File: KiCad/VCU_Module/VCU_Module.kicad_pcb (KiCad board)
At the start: 4 copper layers, 85.1 x 64.6 mm, 44 parts, among them IC1 STM32C092RCT6, J1 5810132011, J11 Conn_ST_STDC14, J5 pin header, J7 5V, J8 3V3, J9 GND, Q1 AO3401A, SW2 SW_Push, U1 OKI-78SR-5_1.5-W36-C, U2 TLV75533PDBV, U6 MCP2562FDT-H_SN

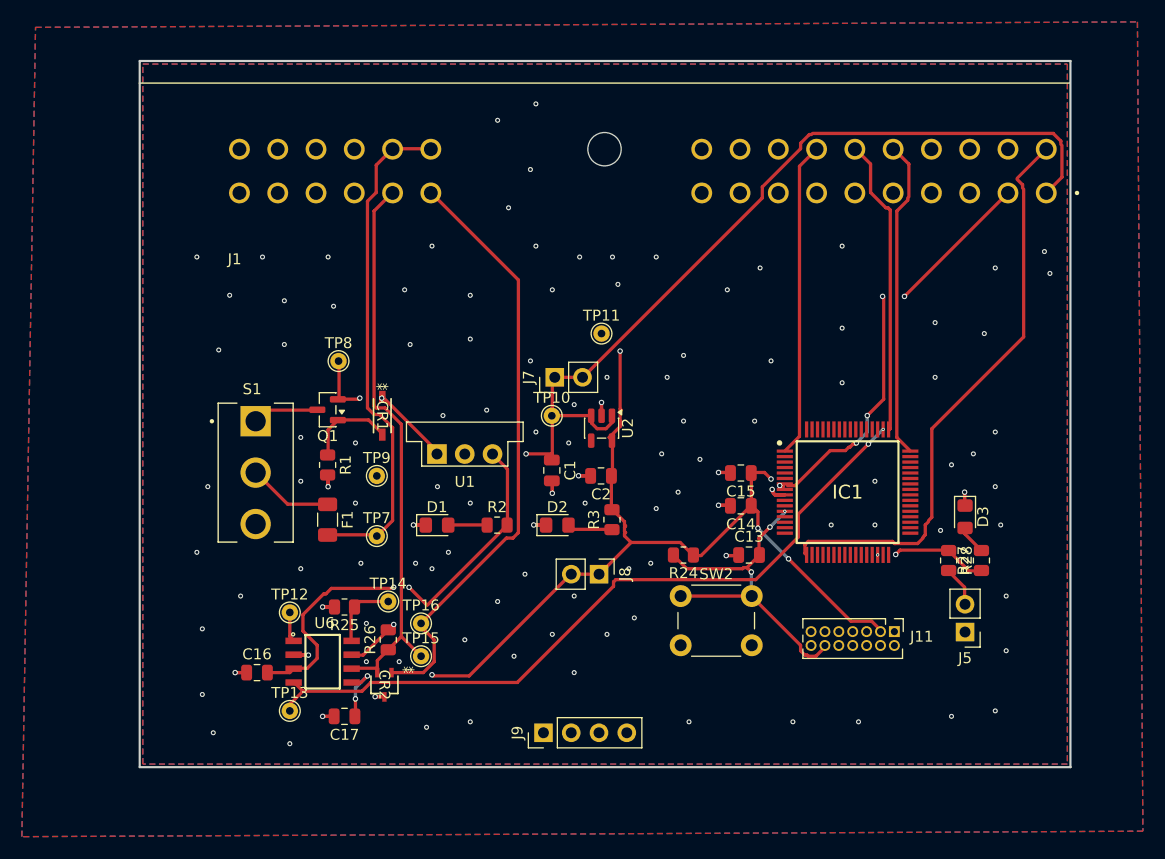
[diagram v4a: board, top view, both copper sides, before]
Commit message: fixed all socket header connections, placed and routed every component on PCB, added all 3d models to footprints
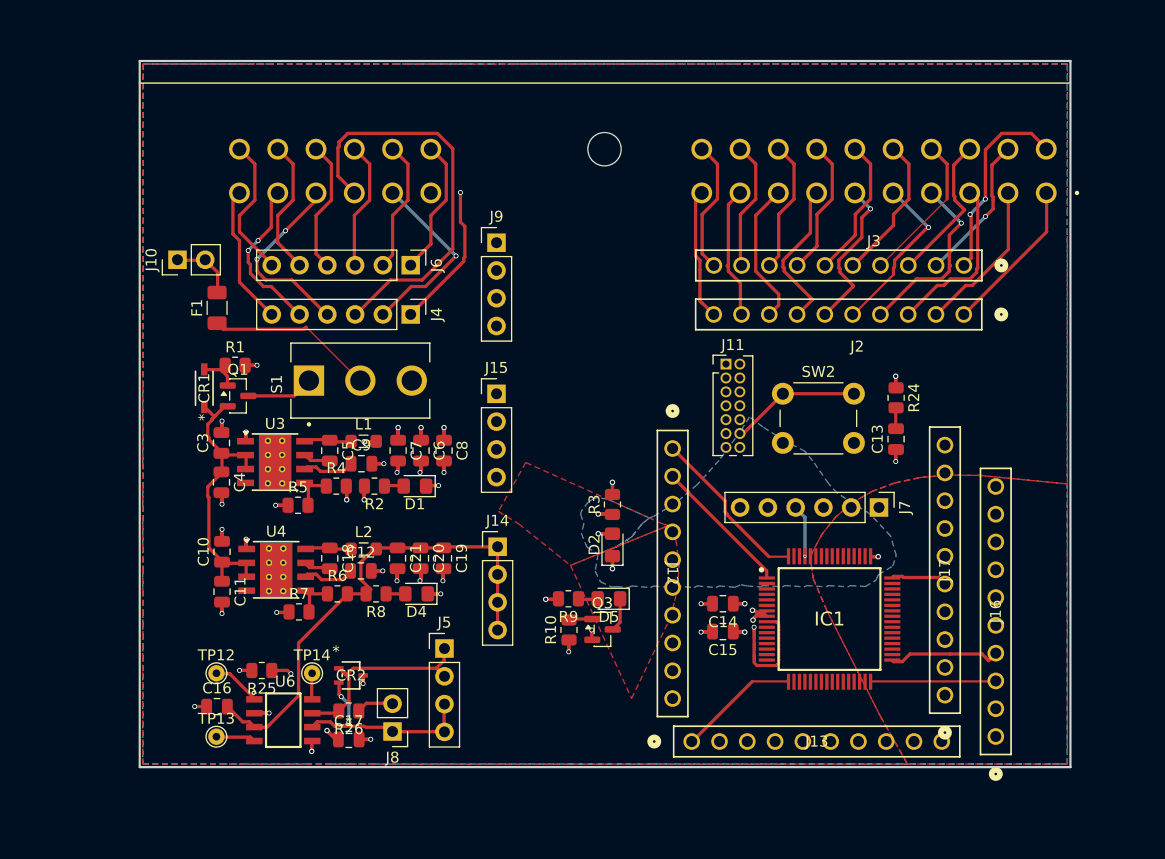
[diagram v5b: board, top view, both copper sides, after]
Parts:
- removed C1, C2: 10u, Capacitor_SMD:C_0805_2012Metric
- removed D3: LED, LED_SMD:LED_0805_2012Metric_Pad1.15x1.40mm_HandSolder
- removed R27, R28: 1k, Resistor_SMD:R_0805_2012Metric
- removed TP10, TP11, TP15, TP16, TP7, TP8, TP9: TestPoint_Small, TestPoint:TestPoint_THTPad_D1.5mm_Drill0.7mm
- removed U1: OKI-78SR-5_1.5-W36-C, Converter_DCDC:Converter_DCDC_Murata_OKI-78SR_Vertical
- removed U2: TLV75533PDBV, Package_TO_SOT_SMD:SOT-23-5
- added C10: 10u, Capacitor_SMD:C_0805_2012Metric, F.Cu at (182.8, 88.5)
- added C11: 220n, Capacitor_SMD:C_0805_2012Metric, F.Cu at (182.8, 92.1)
- added C12: 1u, Capacitor_SMD:C_0805_2012Metric, F.Cu at (195.5, 90.2)
- added C18: 0.1u, Capacitor_SMD:C_0805_2012Metric, F.Cu at (192.7, 89.0)
- added C19: 22u, Capacitor_SMD:C_0805_2012Metric, F.Cu at (203.1, 89.0)
- added C20: 22u, Capacitor_SMD:C_0805_2012Metric, F.Cu at (200.9, 89.0)
- added C21: 22u, Capacitor_SMD:C_0805_2012Metric, F.Cu at (198.8, 89.0)
- added C3: 10u, Capacitor_SMD:C_0805_2012Metric, F.Cu at (182.8, 78.5)
- added C4: 220n, Capacitor_SMD:C_0805_2012Metric, F.Cu at (182.8, 82.1)
- added C5: 0.1u, Capacitor_SMD:C_0805_2012Metric, F.Cu at (192.7, 79.2)
- added C6: 22u, Capacitor_SMD:C_0805_2012Metric, F.Cu at (201.0, 79.2)
- added C7: 22u, Capacitor_SMD:C_0805_2012Metric, F.Cu at (198.9, 79.2)
- added C8: 22u, Capacitor_SMD:C_0805_2012Metric, F.Cu at (203.1, 79.2)
- added C9: 1u, Capacitor_SMD:C_0805_2012Metric, F.Cu at (195.6, 80.4)
- added D4: GRN, LED_SMD:LED_0805_2012Metric_Pad1.15x1.40mm_HandSolder, F.Cu at (200.6, 92.3)
- added D5: GRN, LED_SMD:LED_0805_2012Metric_Pad1.15x1.40mm_HandSolder, F.Cu at (218.2, 92.8)
- added J10: 12V, Connector_PinHeader_2.54mm:PinHeader_1x02_P2.54mm_Vertical, F.Cu at (178.7, 61.8)
- added J12: MCU1, VMS_Footprints:1x10_Header_f, F.Cu at (224.0, 79.0)
- added J13: MCU2, VMS_Footprints:1x10_Header_f, F.Cu at (225.8, 105.8)
- added J14: 5V, Connector_PinHeader_2.54mm:PinHeader_1x04_P2.54mm_Vertical, F.Cu at (208.0, 88.0)
- added J15: 3V3, Connector_PinHeader_2.54mm:PinHeader_1x04_P2.54mm_Vertical, F.Cu at (207.9, 74.0)
- added J16: MCU3, VMS_Footprints:1x10_Header_f, F.Cu at (253.6, 105.3)
- added J17: MCU4, VMS_Footprints:1x10_Header_f, F.Cu at (248.9, 101.6)
- added J2: CN1, VMS_Footprints:1x10_Header_f, F.Cu at (250.6, 66.8)
- added J3: CN2, VMS_Footprints:1x10_Header_f, F.Cu at (250.6, 62.3)
- added J4: CN3, Connector_PinHeader_2.54mm:PinHeader_1x06_P2.54mm_Vertical, F.Cu at (200.1, 66.8)
- added J6: CN4, Connector_PinHeader_2.54mm:PinHeader_1x06_P2.54mm_Vertical, F.Cu at (200.1, 62.2)
- added L1: 3.3u, Inductor_SMD:L_0805_2012Metric_Pad1.05x1.20mm_HandSolder, F.Cu at (195.8, 78.3)
- added L2: 3.3u, Inductor_SMD:L_0805_2012Metric_Pad1.05x1.20mm_HandSolder, F.Cu at (195.8, 88.2)
- added Q3: 2N7002, Package_TO_SOT_SMD:SOT-23, F.Cu at (217.6, 95.5)
- added R10: 1M, Resistor_SMD:R_0805_2012Metric, F.Cu at (214.5, 95.6)
- added R4: 100k, Resistor_SMD:R_0805_2012Metric, F.Cu at (193.2, 82.5)
- added R5: 43.2k, Resistor_SMD:R_0805_2012Metric, F.Cu at (189.8, 84.2)
- added R6: 100k, Resistor_SMD:R_0805_2012Metric, F.Cu at (193.3, 92.3)
- added R7: 43.2k, Resistor_SMD:R_0805_2012Metric, F.Cu at (189.8, 94.0)
- added R8: 1k, Resistor_SMD:R_0805_2012Metric, F.Cu at (196.9, 92.3)
- added R9: 680, Resistor_SMD:R_0805_2012Metric, F.Cu at (214.5, 92.8)
- added U3: LMR33640DDDA, Package_SO:Texas_HSOP-8-1EP_3.9x4.9mm_P1.27mm_ThermalVias, F.Cu at (187.7, 80.2)
- added U4: LMR33640DDDA, Package_SO:Texas_HSOP-8-1EP_3.9x4.9mm_P1.27mm_ThermalVias, F.Cu at (187.8, 90.1)
- D2: value GRN -> Blue
- J5: value pin header -> MCU6; footprint Connector_PinHeader_2.54mm:PinHeader_1x02_P2.54mm_Vertical -> Connector_PinHeader_2.54mm:PinHeader_1x04_P2.54mm_Vertical
- J7: value 5V -> MCU5; footprint Connector_PinHeader_2.54mm:PinHeader_1x02_P2.54mm_Vertical -> Connector_PinHeader_2.54mm:PinHeader_1x06_P2.54mm_Vertical
- J8: value 3V3 -> Termination Resistor Jumper
- R3: value 1k -> 360
- moved J5 47.6 mm to (203.1, 97.3), turned to 0 degrees
- moved J9 45.0 mm to (207.9, 60.2), turned to 0 degrees
- moved J7 31.9 mm to (242.9, 84.4), turned to -90 degrees
- moved J11 28.9 mm to (228.9, 71.3), turned to 0 degrees
- moved R24 24.2 mm to (244.4, 74.4), turned to -90 degrees
- moved J8 23.7 mm to (198.4, 104.9), turned to 180 degrees
- moved F1 21.8 mm to (182.3, 66.2), turned to 90 degrees
- moved SW2 20.7 mm to (234.1, 74.0)
- moved C13 17.1 mm to (244.4, 78.2), turned to 90 degrees
- moved CR1 16.5 mm to (181.2, 73.5), turned to 90 degrees
- moved C15 14.6 mm to (228.6, 95.8)
- moved S1 12.7 mm to (195.4, 72.8), turned to 90 degrees
- moved R1 12.4 mm to (184.0, 71.4), turned to 0 degrees
- moved R2 11.8 mm to (196.7, 82.5), turned to 180 degrees
- moved IC1 11.7 mm to (238.3, 94.6)
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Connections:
- net /POWER/VIN_PROTECTED renamed /VIN_PROTECTED
- C13 pad 2: Net-(IC1-PF2-NRST) -> Net-(C13-Pad2)
- D2 pad 1: GND -> /MCU/PC9/User LED 2
- F1 pad 2: +12V -> VDD
- IC1 pad 1: /A17 -> /MCU/PC11/TIM1_CH4
- IC1 pad 13: unconnected-(IC1-PC0-Pad13) -> /MCU/PC0
- IC1 pad 14: unconnected-(IC1-PC1-Pad14) -> /MCU/PC1
- IC1 pad 15: unconnected-(IC1-PC2-Pad15) -> /MCU/PC2
- IC1 pad 16: unconnected-(IC1-PC3-Pad16) -> /MCU/PC3
- IC1 pad 17: /A11 -> /MCU/PA0/ADC0
- IC1 pad 18: /A12 -> /MCU/PA1/ADC1
- IC1 pad 2: unconnected-(IC1-PC12-Pad2) -> /MCU/PC12
- IC1 pad 21: /A13 -> /MCU/PA4/ADC4
- IC1 pad 22: /A8 -> /MCU/PA5/User LED 1
- IC1 pad 23: /A5 -> /MCU/PA6/SPI1_MISO
- IC1 pad 24: /A6 -> /MCU/PA7/SPI1_MOSI
- IC1 pad 25: /A19 -> /MCU/PC4/TIM2_CH1
- IC1 pad 26: /A20 -> /MCU/PC5/TIM2_CH2
- IC1 pad 27: unconnected-(IC1-PB0-Pad27) -> /MCU/PB0
- IC1 pad 28: unconnected-(IC1-PB1-Pad28) -> /MCU/PB1
- IC1 pad 29: unconnected-(IC1-PB2-Pad29) -> /MCU/PB2
- IC1 pad 3: /A18 -> /MCU/PC13/TIM1_ETR/BKIN
- IC1 pad 30: Net-(IC1-PB10) -> unconnected-(IC1-PB10-Pad30)
- IC1 pad 31: unconnected-(IC1-PB11-Pad31) -> /MCU/PB11
- IC1 pad 32: unconnected-(IC1-PB12-Pad32) -> /MCU/PB12
- IC1 pad 33: unconnected-(IC1-PB13-Pad33) -> /MCU/PB13
- IC1 pad 34: unconnected-(IC1-PB14-Pad34) -> /MCU/PB14
- IC1 pad 35: unconnected-(IC1-PB15-Pad35) -> /MCU/PB15
- IC1 pad 36: /A14 -> /MCU/PA8/ADC8
- IC1 pad 37: /A3 -> /MCU/PA9/I2C1_SCL
- IC1 pad 38: unconnected-(IC1-PC6-Pad38) -> /MCU/PC6
- IC1 pad 39: unconnected-(IC1-PC7-Pad39) -> /MCU/PC7
- IC1 pad 4: unconnected-(IC1-PC14-OSCX_IN-Pad4) -> /MCU/PC14
- IC1 pad 40: unconnected-(IC1-PD8-Pad40) -> /MCU/PD8
- IC1 pad 41: unconnected-(IC1-PD9-Pad41) -> /MCU/PD9
- IC1 pad 42: /A4 -> /MCU/PA10/I2C1_SDA
- IC1 pad 47: /A7 -> /MCU/PA15/SPI1_NSS
- IC1 pad 48: /A15 -> /MCU/PC8/TIM1_CH1
- IC1 pad 49: /A16 -> /MCU/PC9/User LED 2
- IC1 pad 5: unconnected-(IC1-PC15-OSCX_OUT-Pad5) -> /MCU/PC15
- IC1 pad 53: unconnected-(IC1-PD3-Pad53) -> /MCU/PD3
- IC1 pad 54: unconnected-(IC1-PD4-Pad54) -> /MCU/PD4
- IC1 pad 55: unconnected-(IC1-PD5-Pad55) -> /MCU/PD5
- IC1 pad 56: unconnected-(IC1-PD6-Pad56) -> /MCU/PD6
- IC1 pad 58: unconnected-(IC1-PB4-Pad58) -> /MCU/PB4
- IC1 pad 59: unconnected-(IC1-PB5-Pad59) -> /MCU/PB5
- IC1 pad 60: /MCU/GPIO_SPARE1_PB6 -> /MCU/PB6/GPIO_SPARE1
- IC1 pad 61: /MCU/GPIO_SPARE2_PB7 -> /MCU/PB7/GPIO_SPARE2
- IC1 pad 62: /MCU/GPIO_SPARE3_PB8 -> /MCU/PB8/GPIO_SPARE3
- IC1 pad 63: /MCU/GPIO_SPARE4_PB9 -> /MCU/PB9/GPIO_SPARE4
- IC1 pad 64: unconnected-(IC1-PC10-Pad64) -> /MCU/PC10
- J1 pad A1: +5V -> Net-(J2-Pin_1)
- J1 pad A10: GND -> Net-(J2-Pin_10)
- J1 pad A11: /A11 -> Net-(J3-Pin_1)
- J1 pad A12: /A12 -> Net-(J3-Pin_2)
- J1 pad A13: /A13 -> Net-(J3-Pin_3)
- J1 pad A14: /A14 -> Net-(J3-Pin_4)
- J1 pad A15: /A15 -> Net-(J3-Pin_5)
- J1 pad A16: /A16 -> Net-(J3-Pin_6)
- J1 pad A17: /A17 -> Net-(J3-Pin_7)
- J1 pad A18: /A18 -> Net-(J3-Pin_8)
- J1 pad A19: /A19 -> Net-(J3-Pin_9)
- J1 pad A2: +3V3 -> Net-(J2-Pin_2)
- J1 pad A20: /A20 -> Net-(J3-Pin_10)
- J1 pad A3: /A3 -> Net-(J2-Pin_3)
- J1 pad A4: /A4 -> Net-(J2-Pin_4)
- J1 pad A5: /A5 -> Net-(J2-Pin_5)
- J1 pad A6: /A6 -> Net-(J2-Pin_6)
- J1 pad A7: /A7 -> Net-(J2-Pin_7)
- J1 pad A8: /A8 -> Net-(J2-Pin_8)
- J1 pad A9: GND -> Net-(J2-Pin_9)
- J1 pad B1: /MCU/CANH -> Net-(J4-Pin_1)
- J1 pad B10: unconnected-(J1-PadB10) -> Net-(J6-Pin_4)
- J1 pad B11: GND -> Net-(J6-Pin_5)
- J1 pad B12: GND -> Net-(J6-Pin_6)
- J1 pad B2: /MCU/CANL -> Net-(J4-Pin_2)
- J1 pad B3: /MCU/GPIO_SPARE1_PB6 -> Net-(J4-Pin_3)
- J1 pad B4: /MCU/GPIO_SPARE2_PB7 -> Net-(J4-Pin_4)
- J1 pad B5: /MCU/GPIO_SPARE4_PB9 -> Net-(J4-Pin_5)
- J1 pad B6: /MCU/GPIO_SPARE3_PB8 -> Net-(J4-Pin_6)
- J1 pad B7: +12V -> Net-(J6-Pin_1)
- J1 pad B8: +12V -> Net-(J6-Pin_2)
- J1 pad B9: unconnected-(J1-PadB9) -> Net-(J6-Pin_3)
- J5 pad 1: GND -> /MCU/CANH
- J5 pad 2: /MCU/FAULT_LED -> /MCU/CANH
- J7 pad 1: +5V -> /MCU/PB4
- J7 pad 2: +5V -> /MCU/PB5
- J8 pad 1: +3V3 -> /MCU/CANL
- J8 pad 2: +3V3 -> Net-(J8-Pin_2)
- R2 pad 2: +5V -> +3V3
- R24 pad 2: Net-(IC1-PF2-NRST) -> Net-(C13-Pad2)
- R26 pad 1: /MCU/CANL -> Net-(J8-Pin_2)
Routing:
- net +3V3: track 133.0 -> 18.1 mm, vias 12 -> 15
- net +5V: track 122.3 -> 45.7 mm, vias 3 -> 0
- net /MCU/CAN_RXD: track 67.8 -> 3.71 mm, vias 2 -> 0
- net /A11: track 52.6 -> 0.00 mm
- net +12V: track 46.1 -> 0.00 mm
- net /MCU/CANH: track 62.3 -> 19.0 mm, vias 1 -> 0
- net Net-(J4-Pin_3): track 0.00 -> 37.2 mm
- net /MCU/CANL: track 52.1 -> 19.7 mm, vias 0 -> 2
- net /A15: track 29.1 -> 0.00 mm
- net /A17: track 28.9 -> 0.00 mm
- net /A16: track 27.2 -> 0.00 mm
- net Net-(IC1-PF2-NRST): track 32.8 -> 12.0 mm, vias 3 -> 0
- net Net-(J3-Pin_1): track 0.00 -> 18.3 mm, vias 0 -> 2
- net Net-(J4-Pin_4): track 0.00 -> 17.5 mm, vias 0 -> 2
- net Net-(J4-Pin_2): track 0.00 -> 17.1 mm, vias 0 -> 1
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- added copper zone on B.Cu, net +3V3
- added copper zone on F.Cu, net +3V3
- added copper zone on B.Cu, net /MCU/PC9/User LED 2
- added copper zone on F.Cu, net /MCU/PC9/User LED 2
- added copper zone on B.Cu, net Net-(D2-A)
- added copper zone on F.Cu, net Net-(D2-A)
- removed copper zone on B.Cu, net (none)
- removed copper zone on F.Cu, net (none)
- removed copper zone on F.Cu, net GND

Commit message: updated pcb from sohams adjustments to schematic
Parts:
- removed S1: 100SP1T1B4M2QE, VMS_Footprints:SW_100SP1T1B4M2QE
- CR1: value MMSZ5245B-7-F -> MMSZ5240B
- Q1: value AO3401A -> SUD19P06-60; footprint Package_TO_SOT_SMD:SOT-23 -> Package_TO_SOT_SMD:TO-252-2
- R7: value 43.2k -> 24.9k
- moved Q1 8.78 mm to (192.9, 72.7)
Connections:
- CR1 pad 1: /VIN_PROTECTED -> Net-(Q1-S)
- F1 pad 1: Net-(F1-Pad1) -> Net-(Q1-S)
- Q1 pad 3: Net-(Q1-D) -> Net-(Q1-S)
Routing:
- net GND: track 35.4 -> 156.2 mm, vias 30 -> 8
- net /MCU/PC9/User LED 2: track 1.85 -> 29.2 mm
- net +3V3: track 18.1 -> 0.00 mm, vias 15 -> 0
- net Net-(F1-Pad1): track 15.4 -> 0.00 mm
- net /MCU/PC6: track 0.00 -> 15.1 mm, vias 0 -> 2
- net Net-(Q1-S): track 0.00 -> 14.8 mm, vias 0 -> 2
- net Net-(Q1-G): track 3.81 -> 18.2 mm
- net /MCU/PD5: track 0.00 -> 13.0 mm, vias 0 -> 2
- net /MCU/PA8/ADC8: track 0.00 -> 12.8 mm, vias 0 -> 2
- net /MCU/PD9: track 0.00 -> 11.3 mm, vias 0 -> 2
- net /MCU/PC13/TIM1_ETR/BKIN: track 0.00 -> 10.8 mm, vias 0 -> 2
- net /MCU/PB14: track 0.00 -> 10.6 mm, vias 0 -> 2
- net /VIN_PROTECTED: track 27.2 -> 37.5 mm
- net /MCU/PC3: track 0.00 -> 10.1 mm
- net /MCU/PC0: track 0.00 -> 9.39 mm, vias 0 -> 2
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
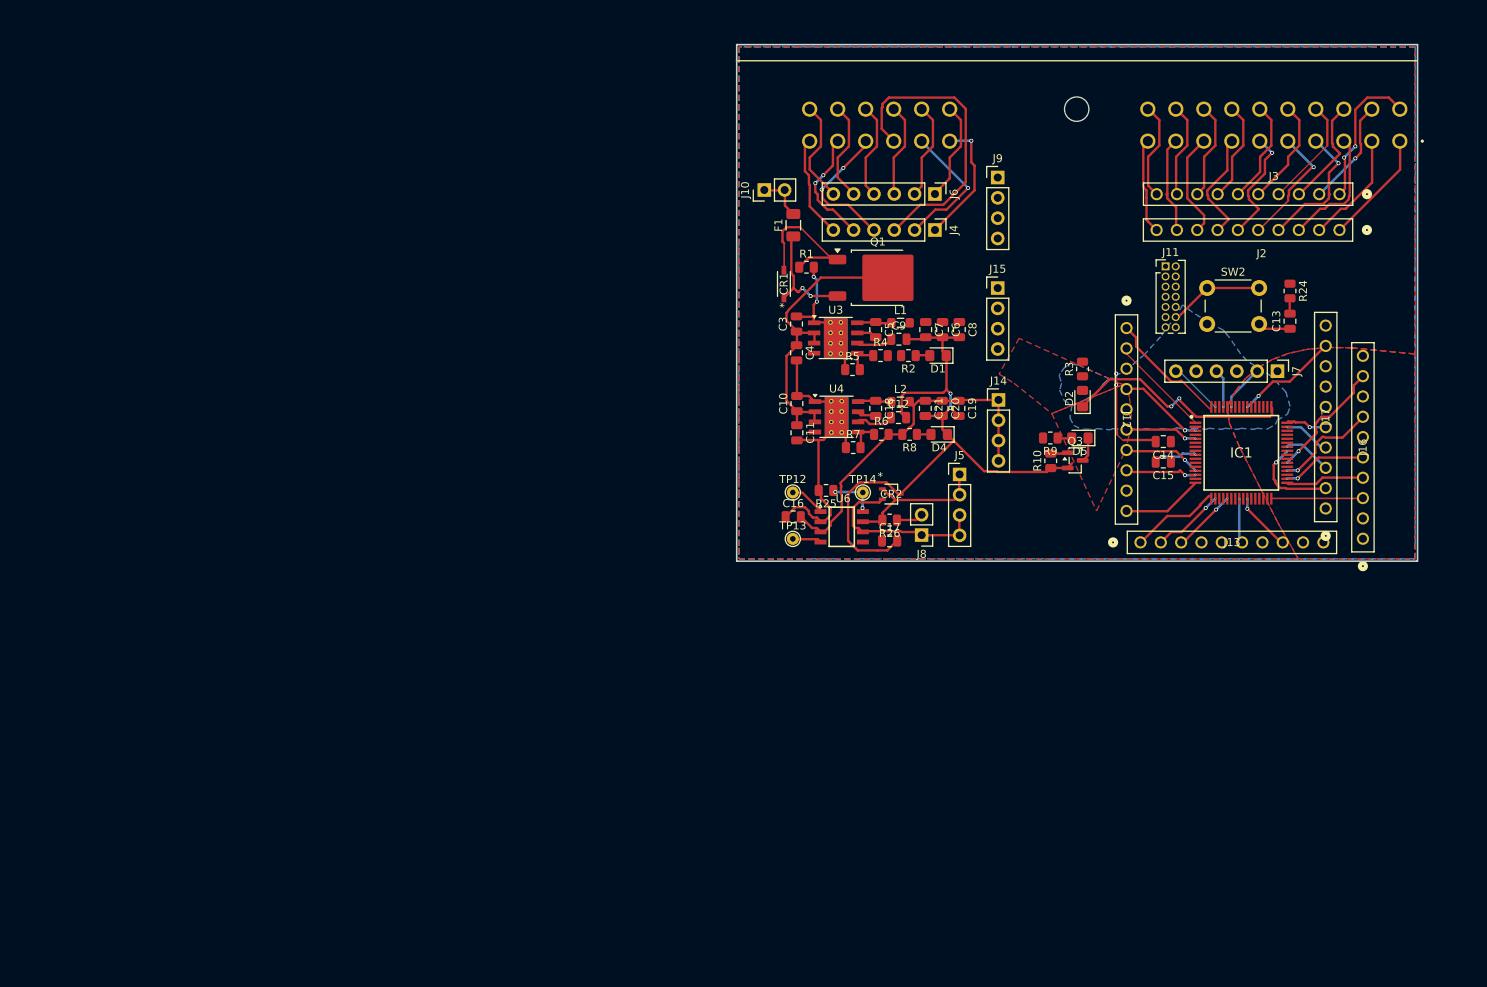
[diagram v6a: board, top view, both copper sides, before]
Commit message: schematic complete with new fuse holder and specs, just need to run ERC once more PCB component placement and traces done, still need to fix some DRC Errors and check warnings Still need to ensure all components are labeled properly with no overlapping silkscreen labels
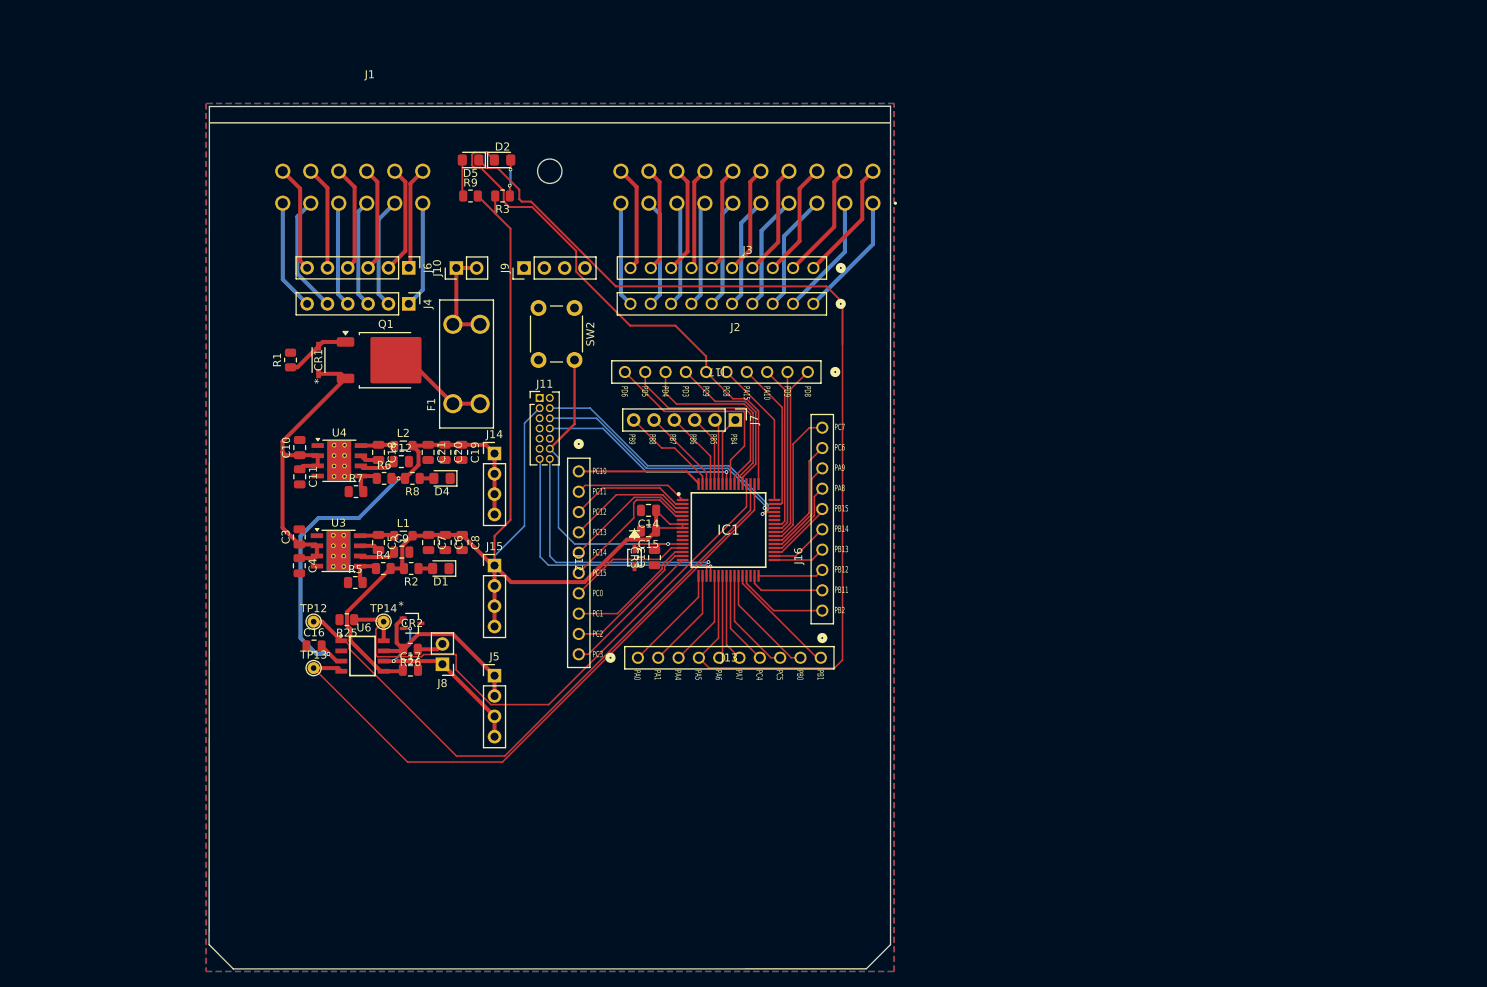
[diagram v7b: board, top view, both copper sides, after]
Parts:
- removed Q3: 2N7002, Package_TO_SOT_SMD:SOT-23
- removed R10: 1M, Resistor_SMD:R_0805_2012Metric
- removed R24: 10k, Resistor_SMD:R_0805_2012Metric
- added CR3: ESDA051-1JY, VMS_Footprints:ESDA051-1JY, F.Cu at (162.5, 107.7)
- F1: value Fuse -> 3568; footprint Fuse:Fuse_1206_3216Metric -> VMS_Footprints:FUSE_3568
- J1: footprint VMS_Footprints:CINCH_5810132011_30-pin -> VMS_Footprints:Cinch_5810132011_PCB_Header
- moved C13 84.7 mm to (165.0, 107.7)
- moved D5 83.7 mm to (142.0, 58.0)
- moved J11 80.0 mm to (150.6, 87.7)
- moved SW2 79.1 mm to (155.0, 76.5), turned to -90 degrees
- moved R9 78.5 mm to (142.0, 62.5), turned to 0 degrees
- moved D2 78.4 mm to (146.0, 58.0), turned to 0 degrees
- moved R3 75.7 mm to (146.0, 62.5), turned to 180 degrees
- moved J15 71.8 mm to (145.0, 108.7)
- moved J12 70.8 mm to (155.5, 96.9)
- moved J16 68.2 mm to (186.0, 114.3)
- moved J7 68.0 mm to (175.1, 90.5)
- moved C3 67.6 mm to (120.6, 105.1)
- moved C4 67.6 mm to (120.6, 108.7)
- moved C5 67.6 mm to (130.5, 105.8)
- moved C6 67.6 mm to (138.8, 105.8)
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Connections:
- net +3V3 renamed 3V3
- net +5V renamed 5V
- net /MCU/PB3 renamed /MCU/SWO
- net Net-(IC1-PA13) renamed /MCU/SWDIO
- net Net-(IC1-PA14-BOOT0) renamed /MCU/SWCLK/BOOT0
- C13 pad 2: Net-(C13-Pad2) -> /MCU/NRST
- CR1 pad 1: Net-(Q1-S) -> /VIN_PROTECTED
- D5 pad 1: Net-(D5-K) -> /MCU/PA5/User LED 1
- F1 pad 1: Net-(Q1-S) -> Net-(Q1-D)
- IC1 pad 12: Net-(IC1-PF2-NRST) -> /MCU/NRST
- IC1 pad 19: Net-(IC1-PA2) -> /MCU/VCP_TX
- IC1 pad 20: Net-(IC1-PA3) -> /MCU/VCP_RX
- J11 pad 12: Net-(IC1-PF2-NRST) -> /MCU/NRST
- J11 pad 13: Net-(IC1-PA2) -> /MCU/VCP_RX
- J11 pad 14: Net-(IC1-PA3) -> /MCU/VCP_TX
- J13 pad 4: /PA5/SPI1_SCK -> /MCU/PA5/User LED 1
- J17 pad 6: /PC9/TIM1_CH2 -> /MCU/PC9/User LED 2
- Q1 pad 2: /VIN_PROTECTED -> Net-(Q1-D)
- Q1 pad 3: Net-(Q1-S) -> /VIN_PROTECTED
- SW2 pad 1: Net-(IC1-PF2-NRST) -> /MCU/NRST
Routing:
- net GND: track 156.2 -> 0.00 mm, vias 8 -> 0
- net 3V3: track 0.00 -> 152.7 mm
- net /MCU/PA5/User LED 1: track 2.22 -> 128.4 mm
- net /MCU/CAN_RXD: track 3.77 -> 79.9 mm
- net /MCU/CAN_TXD: track 4.56 -> 77.8 mm
- net /MCU/STDBY: track 6.20 -> 74.1 mm, vias 2 -> 0
- net /MCU/NRST: track 0.00 -> 44.7 mm, vias 0 -> 1
- net /MCU/PC9/User LED 2: track 29.2 -> 65.7 mm, vias 2 -> 0
- net /MCU/SWDIO: track 0.00 -> 35.4 mm, vias 0 -> 1
- net /MCU/VCP_RX: track 0.00 -> 35.3 mm, vias 0 -> 1
- net /MCU/VCP_TX: track 0.00 -> 34.2 mm, vias 0 -> 1
- net /MCU/SWCLK/BOOT0: track 0.00 -> 33.0 mm, vias 0 -> 1
- net /MCU/PD6: track 0.00 -> 26.8 mm
- net /MCU/SWO: track 0.00 -> 25.9 mm, vias 0 -> 1
- net /MCU/PD4: track 0.00 -> 24.3 mm
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- added copper zone on F.Cu, net GND
- removed copper zone on B.Cu, net /MCU/PC9/User LED 2
- removed copper zone on F.Cu, net /MCU/PC9/User LED 2
- removed copper zone on B.Cu, net 3V3
- removed copper zone on F.Cu, net 3V3
- removed copper zone on B.Cu, net Net-(D2-A)
- removed copper zone on F.Cu, net Net-(D2-A)
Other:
- board size 85.1 x 64.6 mm -> 85.2 x 107.8 mm
- board text added: "PB1 PB0 PC5 PC4 PA7 PA6 PA5 PA4 PA1 PA0"
- board text added: "PB4 PB5 PB6 PB7 PB8 PB9"
- board text added: "PC10 PC11 PC12 PC13 PC14 PC15 PC0 PC1 PC2 PC3"
- board text added: "PC7 PC6 PA9 PA8 PB15 PB14 PB13 PB12 PB11 PB2"
- board text added: "PD8 PD9 PA10 PA15 PC8 PC9 PD3 PD4 PD5 PD6"
